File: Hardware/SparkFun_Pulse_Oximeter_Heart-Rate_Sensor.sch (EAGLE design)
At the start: 5 parts, among them U1 MAX30101EFD+T, U2 MAX32664GWEA+T, U3 1.8V/100mA

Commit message: Adds a few parts (end of day merge)
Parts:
- added U$2: PAM2401, SparkFun-IC-Power:PAM2401
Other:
- moved on the sheet: U1, U2
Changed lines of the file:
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@@
 <part name="FRAME1" library="SparkFun-Aesthetics" deviceset="FRAME-LETTER" device=""/>
 <part name="U$1" library="SparkX" deviceset="QWIIC_BOARD_OUTLINE" device="NH"/>
+<part name="U3" library="SparkFun-IC-Power" deviceset="V_REG_SP6214" device="-1.8V" value="1.8V/100mA"/>
+<part name="U$2" library="SparkFun-IC-Power" deviceset="PAM2401" device="" value="PAM2401"/>
 <part name="U1" library="temp" deviceset="MAX30101EFD+T" device=""/>
 <part name="U2" library="temp" deviceset="MAX32664GWEA+T" device=""/>
-<part name="U3" library="SparkFun-IC-Power" deviceset="V_REG_SP6214" device="-1.8V" value="1.8V/100mA"/>
 </parts>
 <sheets>
@@
 </instance>
 <instance part="U$1" gate="G$1" x="231.14" y="40.64" smashed="yes"/>
-<instance part="U1" gate="G$1" x="78.74" y="147.32" smashed="yes">
-<attribute name="NAME" x="71.12" y="157.48" size="1.778" layer="95"/>
-<attribute name="VALUE" x="71.12" y="134.62" size="1.778" layer="96"/>
-</instance>
-<instance part="U2" gate="G$1" x="167.64" y="147.32" smashed="yes">
-<attribute name="NAME" x="157.48" y="167.64" size="1.778" layer="95"/>
-<attribute name="VALUE" x="157.48" y="127" size="1.778" layer="96"/>
-</instance>
 <instance part="U3" gate="G$1" x="53.34" y="96.52" smashed="yes">
 <attribute name="NAME" x="45.72" y="104.394" size="1.778" layer="95" font="vector"/>
 <attribute name="VALUE" x="45.72" y="88.646" size="1.778" layer="96" font="vector" align="top-left"/>
 </instance>
+<instance part="U$2" gate="G$1" x="127" y="81.28" smashed="yes">
+<attribute name="NAME" x="121.92" y="95.504" size="1.778" layer="95"/>
+<attribute name="VALUE" x="122.174" y="65.278" size="1.778" layer="96"/>
+</instance>
+<instance part="U1" gate="G$1" x="88.9" y="137.16" smashed="yes">
+<attribute name="NAME" x="78.74" y="147.32" size="1.778" layer="95"/>
+<attribute name="VALUE" x="78.74" y="124.46" size="1.778" layer="96"/>
+</instance>
+<instance part="U2" gate="G$1" x="152.4" y="139.7" smashed="yes">
+<attribute name="NAME" x="142.24" y="160.02" size="1.778" layer="95"/>
+<attribute name="VALUE" x="142.24" y="119.38" size="1.778" layer="96"/>
+</instance>
 </instances>

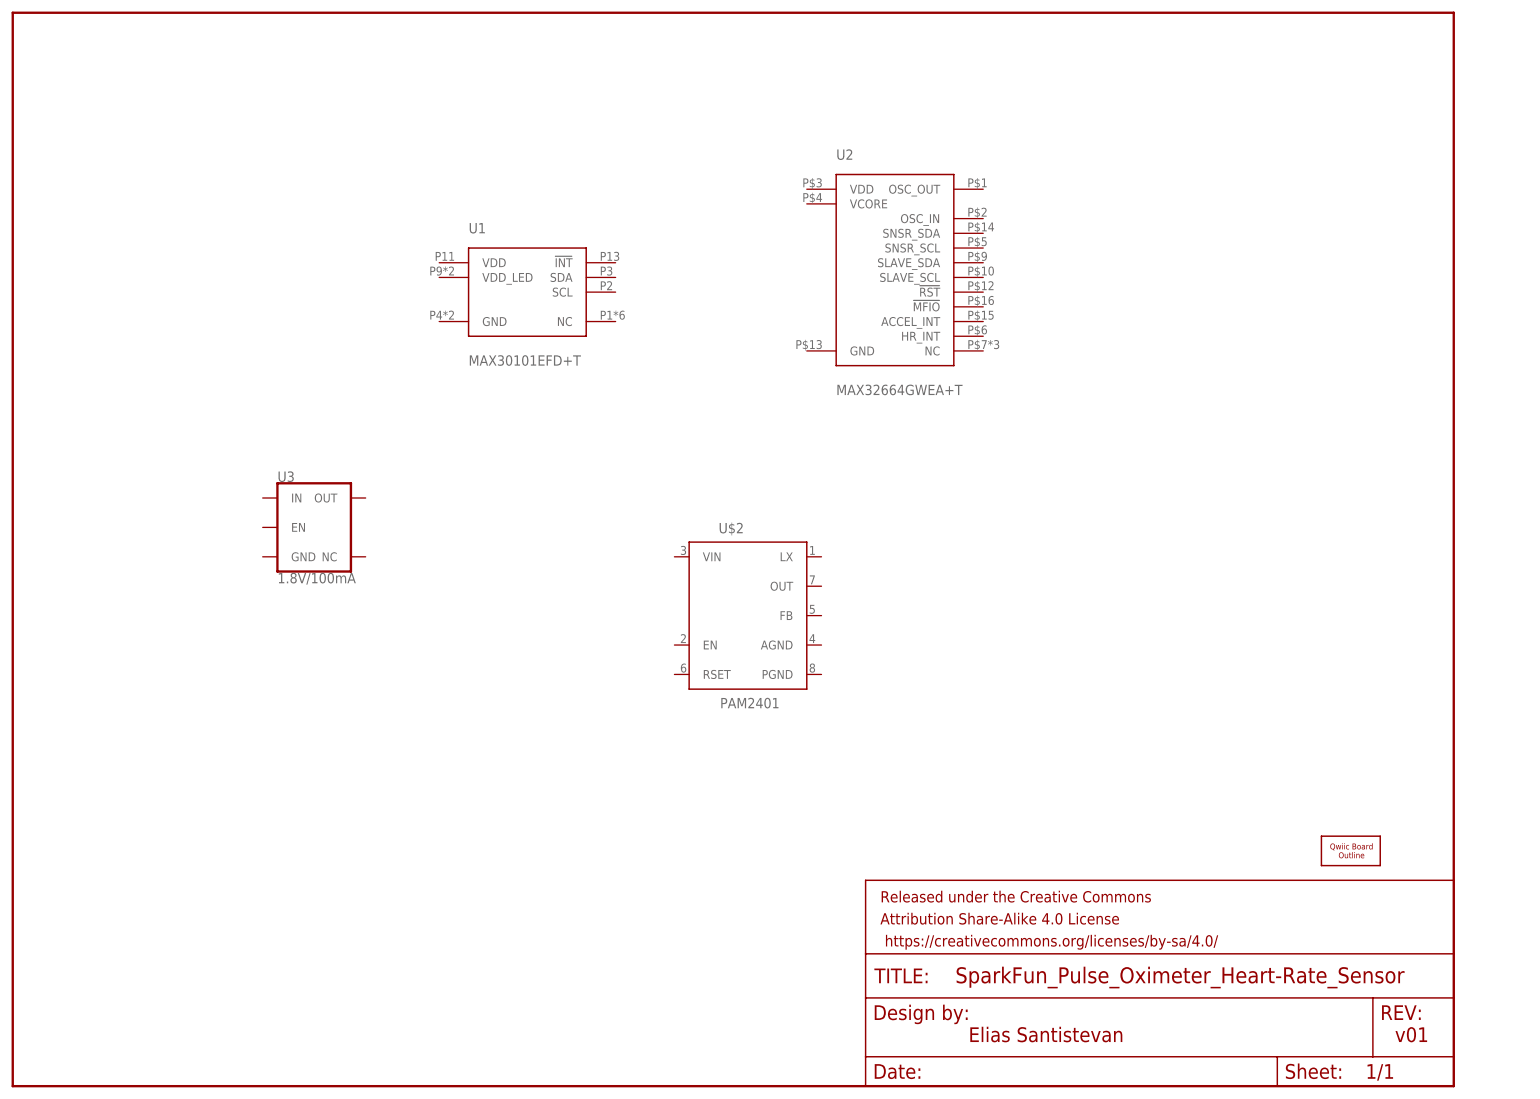
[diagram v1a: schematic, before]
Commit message: Adds parts to DC-DC converter
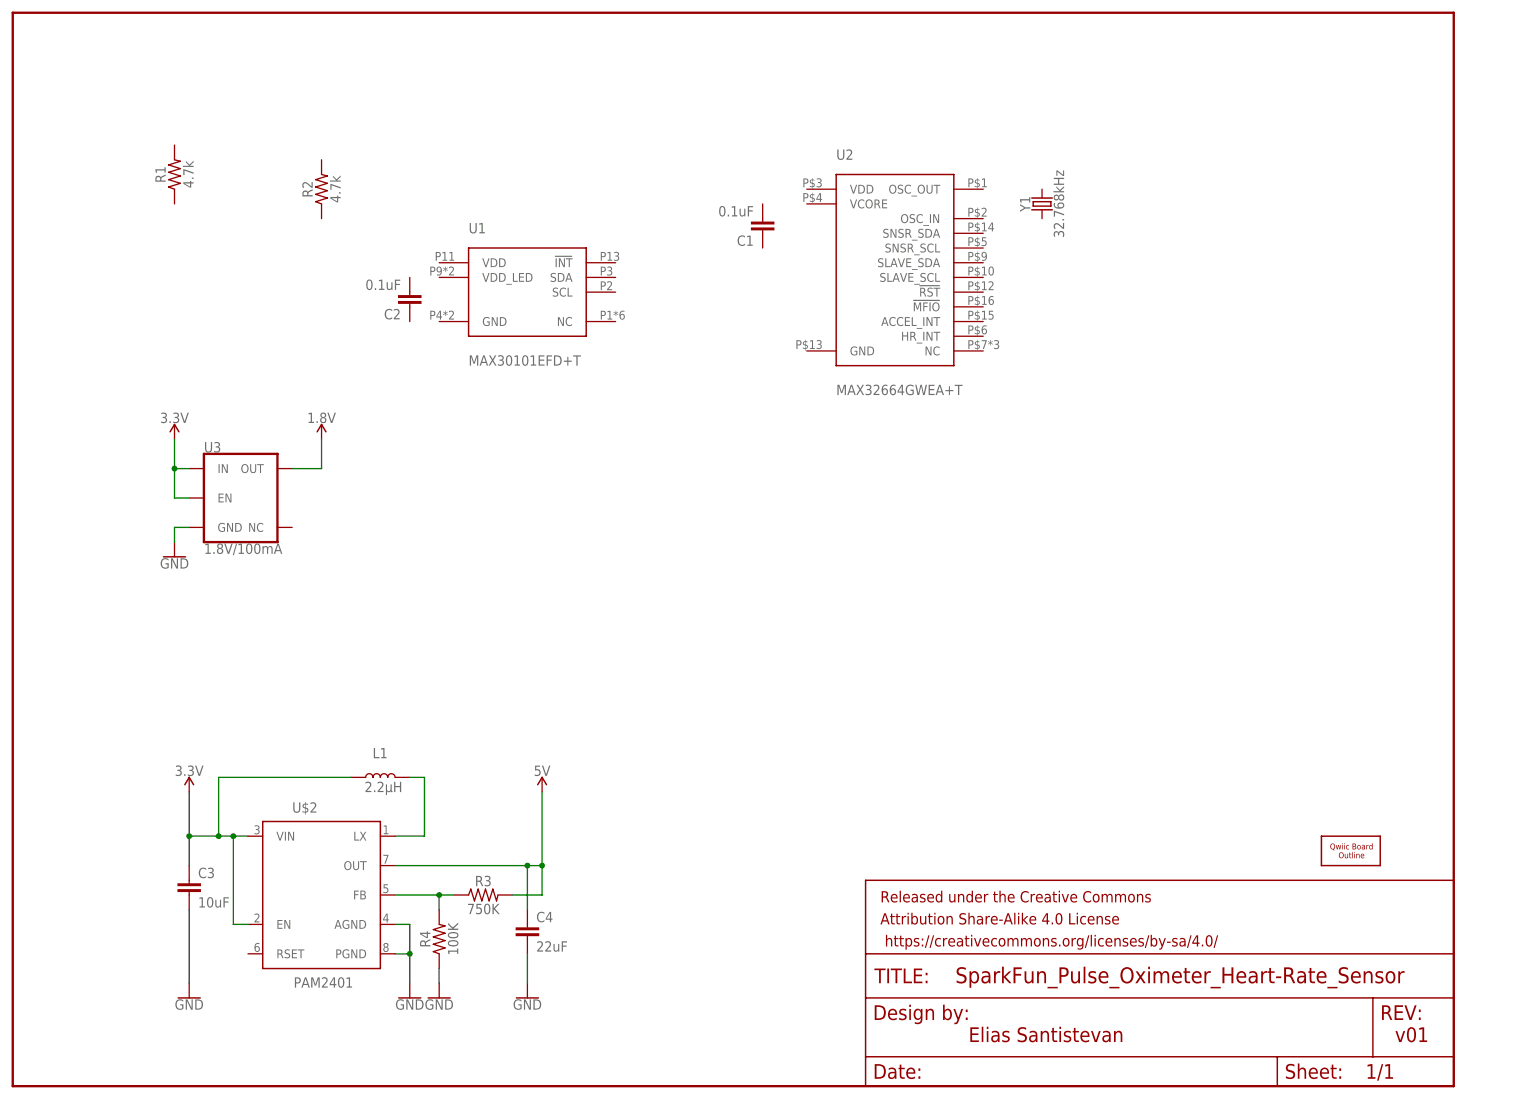
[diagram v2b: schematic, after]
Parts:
- added C1, C2: 0.1uF, SparkFun-Capacitors:0.1UF-0402-16V-10%
- added C3: 10uF, SparkFun-Capacitors:10UF-0603-6.3V-20%
- added C4: 22uF, SparkFun-Capacitors:22UF-0805-6.3V-20%
- added L1: 2.2μH, SparkFun-Coils:2.2μH_SHIELDED_INDUCTOR
- added R1, R2: 4.7k, SparkFun-Resistors:4.7KOHM-0603-1/10W-1%
- added R3: 750K, SparkFun-Resistors:750KOHM-0603-1/10W-1%
- added R4: 100K, SparkFun-Resistors:100KOHM-0402-1/16W-1%
- added Y1: 32.768kHz, SparkFun-Clocks:CRYSTAL-32.768KHZSMD-3.2X1.5
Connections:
- new net 1.8V: U3.OUT
- new net 3.3V: C3.1, L1.1, U$2.EN, U$2.VIN, U3.EN, U3.IN
- new net 5V: C4.1, R3.2, U$2.OUT
- new net GND: C3.2, C4.2, R4.1, U$2.AGND, U$2.PGND, U3.GND
- new net N$2: R3.1, R4.2, U$2.FB
- new net N$3: L1.2, U$2.LX
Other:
- moved on the sheet: U$2, U3

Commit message: Many traces and parts have been added, too many to list.
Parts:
- removed U$1: QWIIC_BOARD_OUTLINENH, SparkX:QWIIC_BOARD_OUTLINENH
- added C5: 1.0uF, SparkFun-Capacitors:1.0UF-0603-16V-10%
- added C6, C7: 1.0uF, SparkFun-Capacitors:1.0UF-0402-16V-10%
- added J1: (no value), SparkFun-Connectors:QWIIC_CONNECTORJS-1MM
- added J3: (no value), SparkFun-Connectors:CONN_041X04_NO_SILK
- added JP1: JUMPER-SMT_3_2-NC_TRACE_SILK, SparkFun-Jumpers:JUMPER-SMT_3_2-NC_TRACE_SILK
- added R5, R6, R7: 4.7k, SparkFun-Resistors:4.7KOHM-0603-1/10W-1%
- C1: value 0.1uF -> 10uF; device SparkFun-Capacitors:0.1UF-0402-16V-10% -> SparkFun-Capacitors:10UF-0603-6.3V-20%
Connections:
- new net !HR_INT: R5.1, U1.!INT, U2.HR_INT
- new net !MFIO: U2.!MFIO
- new net !RST: U2.!RST
- new net HOST_SCL: J1.4, J3.4, R7.1, U2.SLAVE_SCL
- new net HOST_SDA: J1.3, J3.3, R6.1, U2.SLAVE_SDA
- new net N$1: C7.1, U2.VCORE
- new net N$4: JP1.3, R6.2
- new net N$5: JP1.1, R7.2
- new net N$6: U2.OSC_OUT, Y1.1
- new net N$7: U2.OSC_IN, Y1.2
- new net SNSR_SCL: R2.1, U1.SCL, U2.SNSR_SCL
- new net SNSR_SDA: R1.1, U1.SDA, U2.SNSR_SDA
- net 1.8V: now also C2.1, C5.1, C6.1, R1.2, R2.2, R5.2, U1.VDD, U2.VDD
- net 3.3V: now also J1.2, J3.2, JP1.2
- net 5V: now also C1.1, U1.VDD_LED
- net GND: now also C1.2, C2.2, C5.2, C6.2, C7.2, J1.1, J3.1, U1.GND, U2.GND
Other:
- note added: "Address: 0x55"
- note added: "VCC Range: 1.71 - 3.63V"
- moved on the sheet: C1, C2, R1, R2, U1, U3, Y1

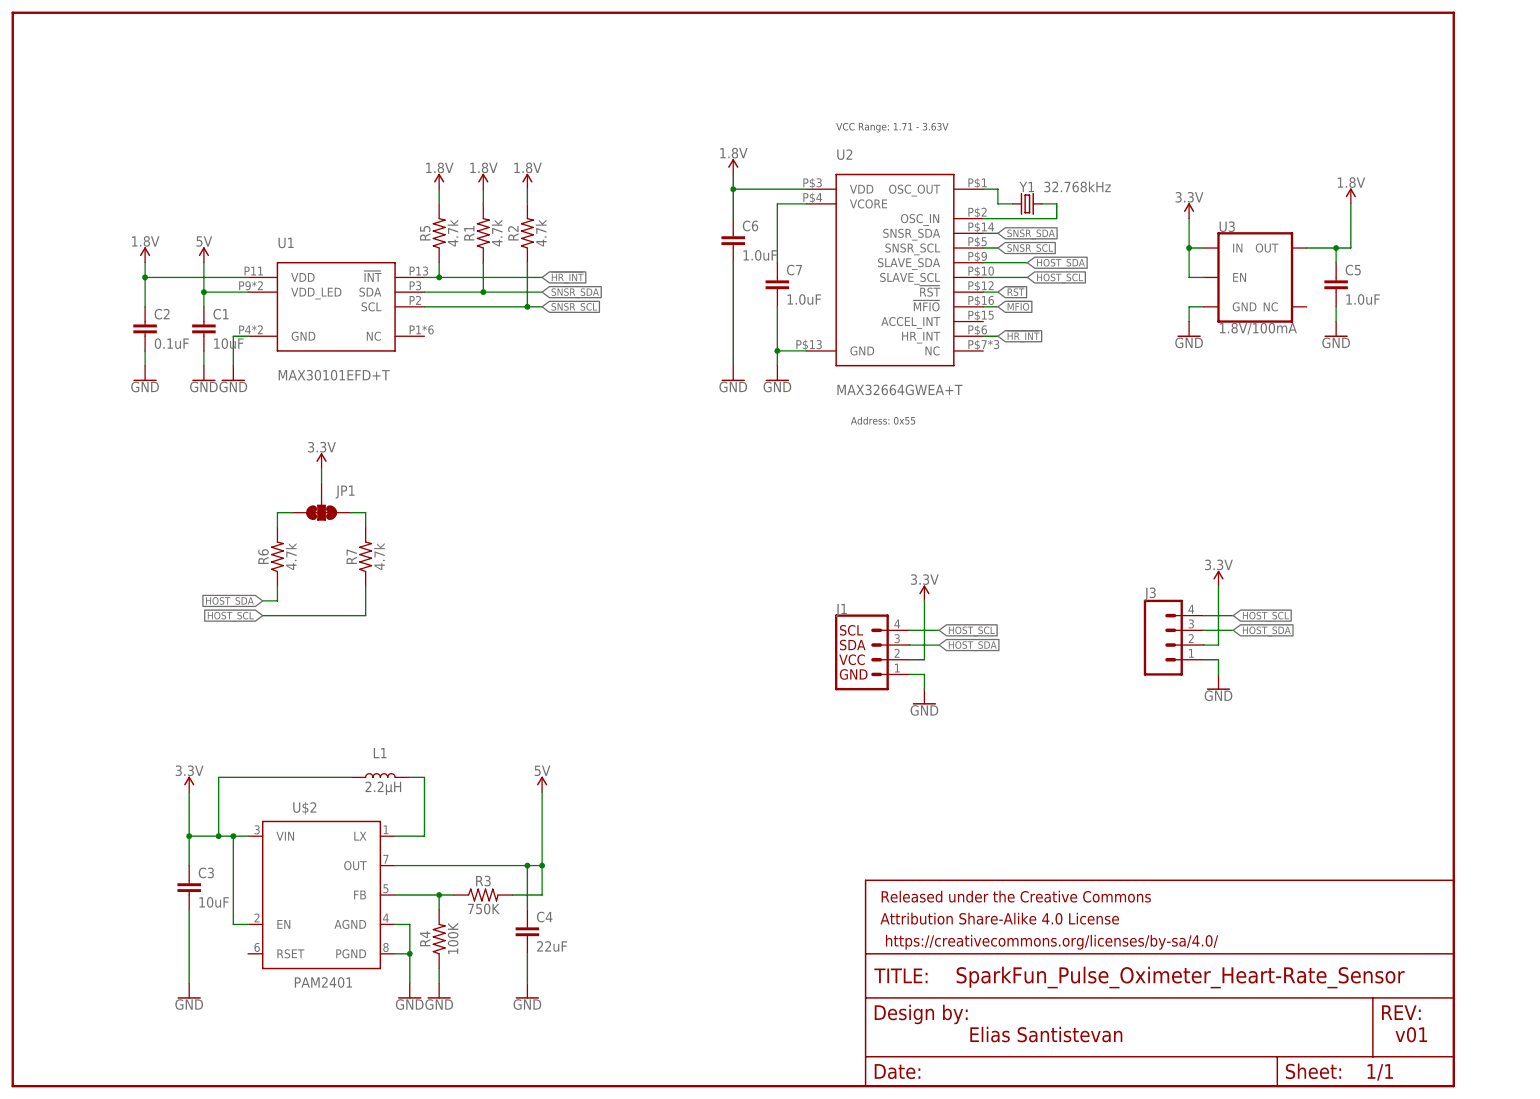
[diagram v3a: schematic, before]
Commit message: Adds slik, trace work complete, ground vias added throughout design, schematic organized with lables
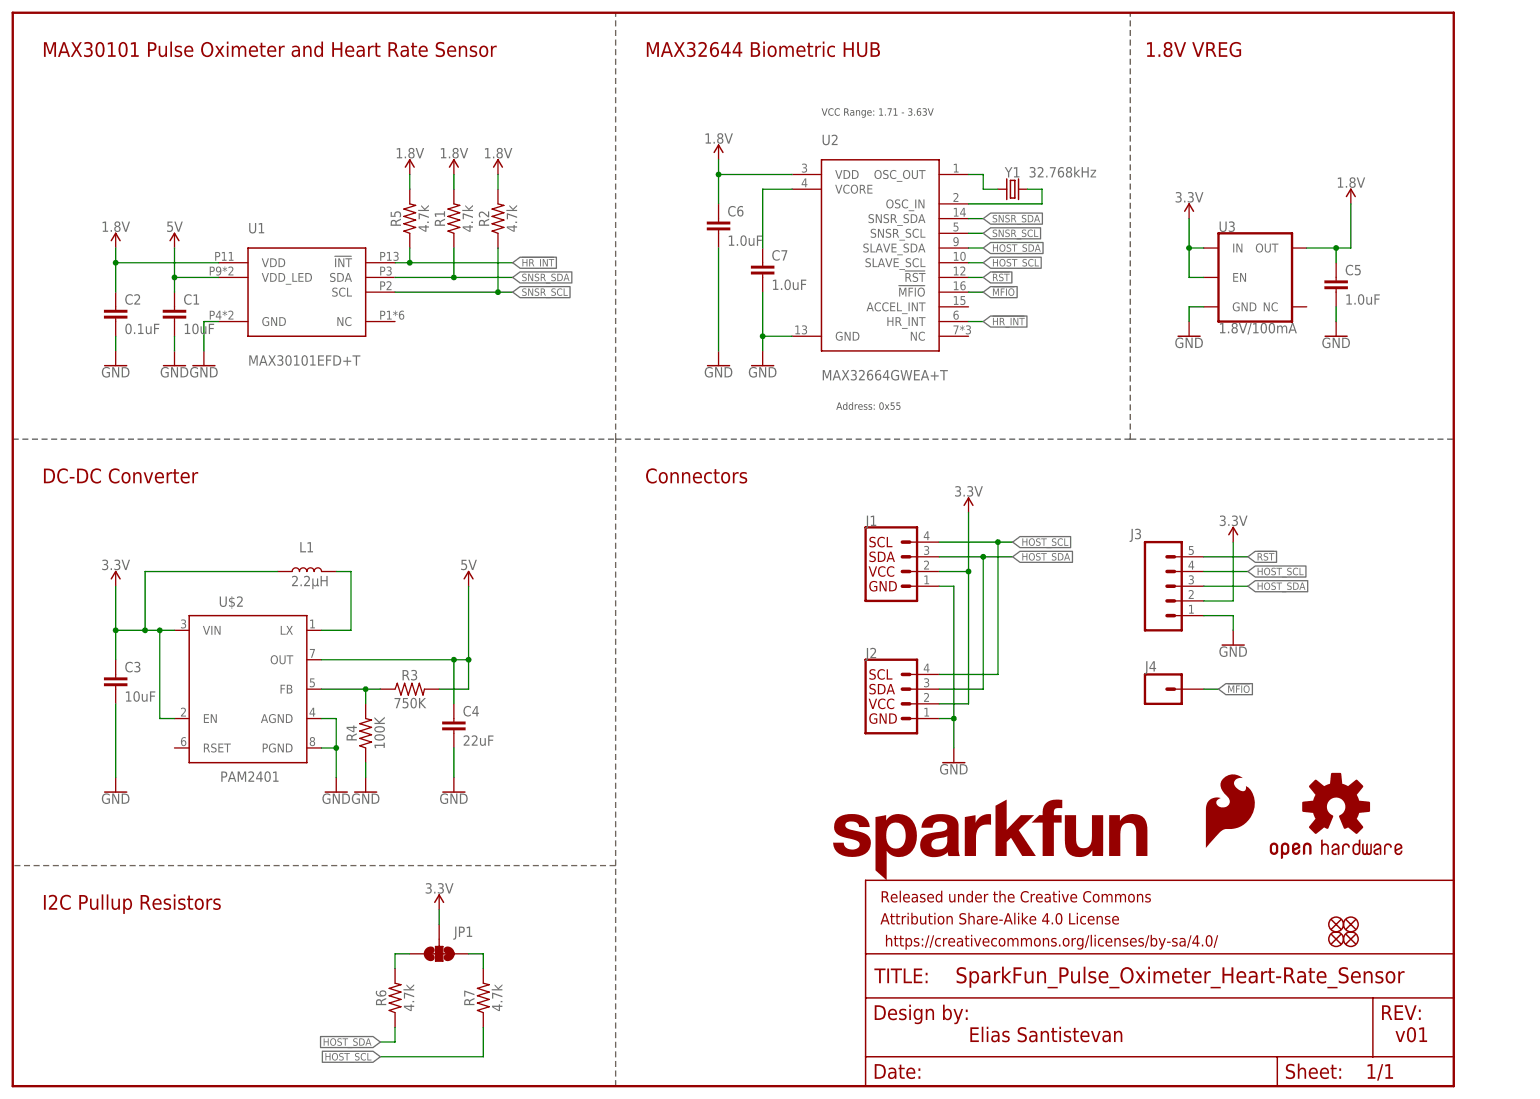
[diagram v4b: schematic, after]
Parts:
- added FD1, FD2, FD3, FD4: FIDUCIALUFIDUCIAL, SparkFun-Aesthetics:FIDUCIALUFIDUCIAL
- added J2: (no value), SparkFun-Connectors:QWIIC_CONNECTORJS-1MM
- added J4: (no value), SparkFun-Connectors:CONN_01PTH_NO_SILK_YES_STOP
- added LOGO1: SFE_LOGO_FLAME.1_INCH, SparkFun-Aesthetics:SFE_LOGO_FLAME.1_INCH
- added LOGO2: OSHW-LOGOMINI, SparkFun-Aesthetics:OSHW-LOGOMINI
- added LOGO3: SFE_LOGO_NAME.1_INCH, SparkFun-Aesthetics:SFE_LOGO_NAME.1_INCH
- J3: device SparkFun-Connectors:CONN_041X04_NO_SILK -> SparkFun-Connectors:CONN_05NO_SILK
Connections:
- net !MFIO: now also J4.1
- net !RST: now also J3.5
- net 3.3V: now also J2.2
- net GND: now also J2.1
- net HOST_SCL: now also J2.4
- net HOST_SDA: now also J2.3
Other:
- note added: "1.8V VREG"
- note added: "Connectors"
- note added: "DC-DC Converter"
- note added: "I2C Pullup Resistors"
- note added: "MAX30101 Pulse Oximeter and Heart Rate Sensor"
- note added: "MAX32644 Biometric HUB"
- moved on the sheet: C1, C2, C3, C4, C6, C7, J1, JP1, L1, R1, R2, R3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

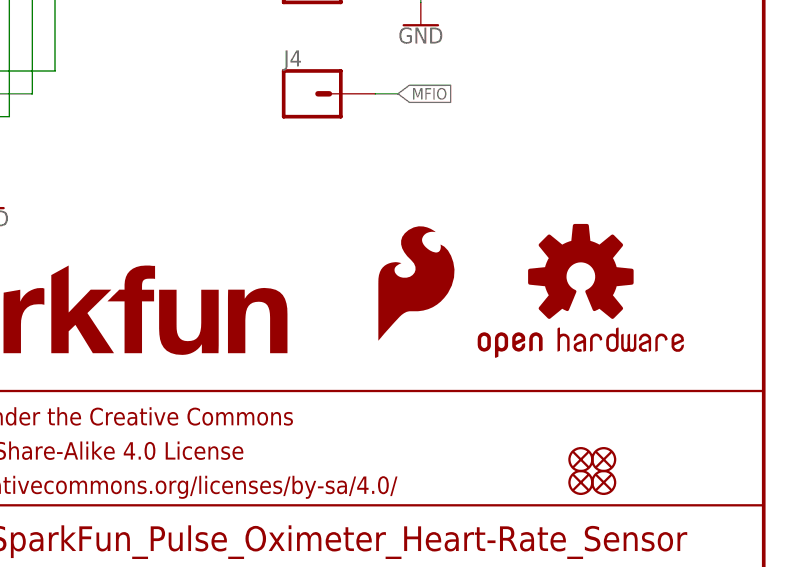
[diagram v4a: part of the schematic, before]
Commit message: Moves silk labels around
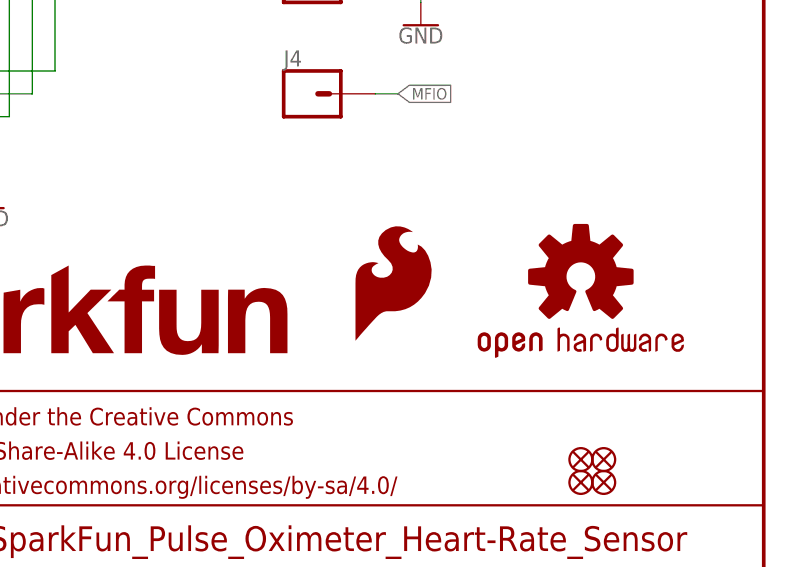
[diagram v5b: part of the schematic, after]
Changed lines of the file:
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@@
 <attribute name="NAME" x="195.58" y="71.628" size="1.778" layer="95" font="vector"/>
 </instance>
-<instance part="LOGO1" gate="G$1" x="205.74" y="40.64" smashed="yes"/>
+<instance part="LOGO1" gate="G$1" x="203.2" y="40.64" smashed="yes"/>
 <instance part="LOGO2" gate="G$1" x="228.6" y="48.26" smashed="yes"/>
 <instance part="LOGO3" gate="G$1" x="139.7" y="35.56" smashed="yes"/>
